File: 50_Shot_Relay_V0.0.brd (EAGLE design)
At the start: 110.7 x 130.5 mm, 183 parts, among them J1 J13, J2 J14, J3 J15, J4 J16, Q1 Qs5U34CT-ND, Q10 Qs5U34CT-ND, Q11 Qs5U34CT-ND, Q12 Qs5U34CT-ND, Q13 Qs5U34CT-ND, Q14 Qs5U34CT-ND, Q15 Qs5U34CT-ND, Q16 Qs5U34CT-ND, Q17 Qs5U34CT-ND, Q18 Qs5U34CT-ND, Q19 Qs5U34CT-ND, Q2 Qs5U34CT-ND, Q20 Qs5U34CT-ND, Q21 Qs5U34CT-ND, Q22 Qs5U34CT-ND, Q23 Qs5U34CT-ND, Q24 Qs5U34CT-ND, Q25 Qs5U34CT-ND, Q26 Qs5U34CT-ND, Q27 Qs5U34CT-ND, Q28 Qs5U34CT-ND, Q29 Qs5U34CT-ND, Q3 Qs5U34CT-ND, Q30 Qs5U34CT-ND, Q4 Qs5U34CT-ND, Q5 Qs5U34CT-ND, Q6 Qs5U34CT-ND, Q7 Qs5U34CT-ND, Q8 Qs5U34CT-ND, Q9 Qs5U34CT-ND, U1 MM74HC595, U2 MM74HC595, U3 7400, U4 MM74HC245, U5 MM74HC245, U6 ULN2803ADW, U7 ULN2803ADW, X1 22-23-2111, X2 22-23-2111, X3 22-23-2091, X4 22-23-2031, X5 22-23-2101, X6 22-23-2101

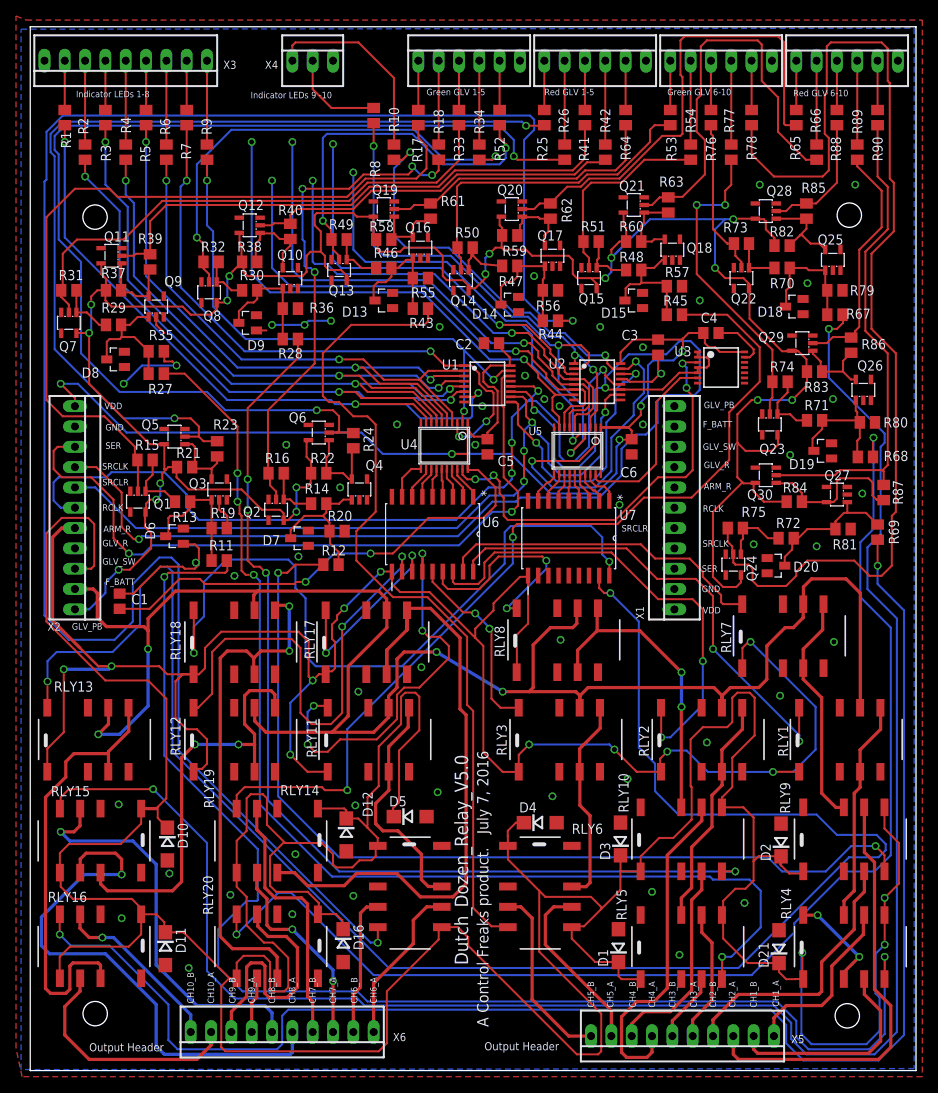
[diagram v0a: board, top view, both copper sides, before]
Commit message: add proper relay board
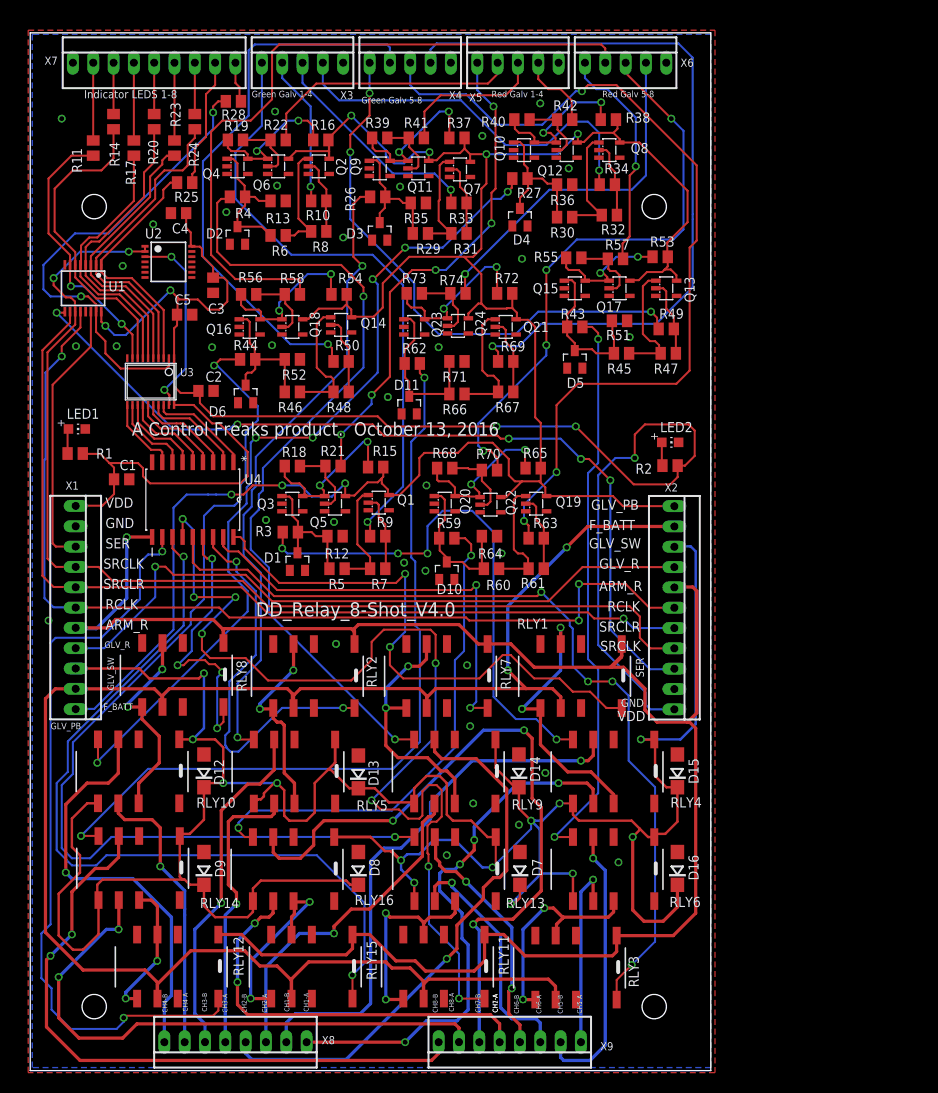
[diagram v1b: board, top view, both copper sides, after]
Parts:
- removed C6: 0.01uF, rcl:C0805
- removed D18, D19, D20: 5.0V, Mine:SOT23
- removed D21: SA2M-E3/5ATGICT-ND, Mine:DO214AC
- removed J1: J13, Mine:22-23-2061
- removed J2: J14, Mine:22-23-2061
- removed J3: J15, Mine:22-23-2061
- removed J4: J16, Mine:22-23-2061
- removed Q25, Q26, Q27, Q28, Q29, Q30: Qs5U34CT-ND, Mine:SOT23-5L
- removed R75: 1M, rcl:M0805
- removed R76, R77, R78, R88, R89, R90: 1k, rcl:M0805
- removed R79, R80, R81, R85, R86, R87: 100k, rcl:M0805
- removed R82, R83, R84: 10k, rcl:M0805
- removed RLY17, RLY18, RLY19, RLY20: OMRON, Mine:OMRONG6S
- removed U5: MM74HC245, Mine:TSSOP20
- removed U6, U7: ULN2803ADW, Texas Instruments_By_element14_Batch_1:SOIC127P1030X265-18N
- added LED1, LED2: LEDCHIP-LED0805, Mine:CHIP-LED0805
- added X7: 22-23-2091, Mine:22-23-2091
- added X8, X9: 22-23-2081, Mine:22-23-2081
- C1: value .01uf -> 0.01uF
- D1, D10, D11, D2, D3, D4, D5: value SA2M-E3/5ATGICT-ND -> 5.0V; device Mine:DO214AC -> Mine:SOT23
- D13, D14, D15, D7, D8, D9: value 5.0V -> SA2M-E3/5ATGICT-ND; device Mine:SOT23 -> Mine:DO214AC
- R1, R2: value 330 -> 100
- R10: value 560 -> 1k
- R11, R28: value 10k -> 330
- R12, R45, R60, R68: value 10k -> 100k
- R14, R20, R23, R24: value 100k -> 330
- R15, R16: value 1M -> 10k
- R17, R25: value 1k -> 330
- R18, R52, R64, R66: value 1k -> 100k
- R21, R22, R58, R69: value 10k -> 1k
- R26, R53, R54, R65: value 1k -> 10k
- R3, R4: value 330 -> 10k
- R47, R48, R61: value 100k -> 1M
- R49, R50, R74: value 1M -> 1k
- R5, R6: value 330 -> 100k
- R51, R73: value 1M -> 100k
- R57, R63, R70: value 100k -> 1k
- R62, R72: value 100k -> 10k
- R67: value 10k -> 1M
- R7: value 330 -> 1M
- R8: value 560 -> 1M
- R9: value 330 -> 1k
- U2: value MM74HC595 -> 7400; device Mine:TSSOP16 -> 74xx-us:TSSOP14
- U3: value 7400 -> MM74HC245; device 74xx-us:TSSOP14 -> Mine:TSSOP20
- U4: value MM74HC245 -> ULN2803ADW; device Mine:TSSOP20 -> Texas Instruments_By_element14_Batch_1:SOIC127P1030X265-18N
- X3: value 22-23-2091 -> 22-23-2051; device Mine:22-23-2091 -> Mine:22-23-2051
- X4: value 22-23-2031 -> 22-23-2051; device Mine:22-23-2031 -> Mine:22-23-2051
- X5, X6: value 22-23-2101 -> 22-23-2051; device con-molex:22-23-2101 -> Mine:22-23-2051
- moved X6 128.5 mm to (74.4, 126.0), turned to 0 degrees
- moved X5 123.4 mm to (61.0, 126.0), turned to 0 degrees
- moved D2 101.6 mm to (25.9, 104.4), turned to 0 degrees
- moved R2 83.0 mm to (80.0, 75.6), turned to 0 degrees
- moved D3 81.7 mm to (43.7, 104.9), turned to 0 degrees
- moved X2 76.0 mm to (80.5, 57.9)
- moved X1 75.9 mm to (5.68, 57.9), turned to 270 degrees
- moved D4 75.7 mm to (61.2, 106.7)
- moved D11 74.5 mm to (47.4, 83.2), turned to 0 degrees
- moved U3 71.4 mm to (15.0, 86.1), turned to 180 degrees
- moved D8 70.5 mm to (41.0, 25.3)
- moved D9 68.4 mm to (21.7, 25.3)
- moved C4 68.2 mm to (18.5, 107.2), turned to 180 degrees
- moved RLY10 64.3 mm to (15.4, 35.6), turned to 180 degrees
- moved D1 62.6 mm to (33.4, 63.6), turned to 0 degrees
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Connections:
- removed net CH10_A: RLY16.6, X6.9
- removed net CH10_B: RLY16.3, X6.10
- removed net CH9_A: RLY20.6, X6.7
- removed net CH9_B: RLY20.3, X6.8
- removed net GLV10_GRN: J2.5, R78.1
- removed net GLV10_RED: J4.5, R90.1
- removed net GLV9_GRN: J2.4, R77.1
- removed net GLV9_RED: J4.4, R89.1
- removed net GLV_10: R69.2, RLY16.4
- removed net GLV_9: R68.2, RLY20.4
- removed net N$101: RLY18.3, RLY18.5, RLY20.7
- removed net N$162: D19.3, Q26.1, R68.1, R71.2, R80.2
- removed net N$163: Q23.1, R71.1, R74.2
- removed net N$164: Q23.2, R74.1, R77.2
- removed net N$165: Q26.5, Q29.1, R83.1, R86.2
- removed net N$166: Q29.2, R86.1, R89.2
- removed net N$169: D20.3, Q27.1, R69.1, R72.2, R81.2
- removed net N$170: Q24.1, R72.1, R75.2
- removed net N$171: Q24.2, R75.1, R78.2
- removed net N$172: Q27.5, Q30.1, R84.1, R87.2
- removed net N$173: Q30.2, R87.1, R90.2
- removed net N$179: R3.1, X3.6
- removed net N$180: R2.1, X3.7
- removed net N$181: R1.1, X3.8
- removed net N$182: R10.1, X4.1
- removed net N$183: R8.1, X4.2
- removed net N$19: R10.2, U2.15, U5.2
- removed net N$20: R8.2, U2.1, U5.3
- removed net N$21: U1.9, U2.14
- removed net N$22: U2.2, U5.4
- removed net N$23: U2.3, U5.5
- removed net N$24: U2.4, U5.6
- removed net N$25: U2.5, U5.7
- removed net N$26: U2.6, U5.8
- removed net N$27: U2.7, U5.9
- removed net N$35: U5.18, U7.1
- removed net N$36: U5.17, U7.2
- removed net N$37: U5.16, U7.3
- removed net N$38: U5.15, U7.4
- removed net N$39: U5.14, U7.5
- removed net N$40: U5.13, U7.6
- removed net N$41: U5.12, U7.7
- removed net N$42: U5.11, U7.8
- removed net N$44: U3.6, U5.19
- removed net N$52: RLY18.8, U7.18
- removed net N$53: RLY13.8, U7.17
- removed net N$54: X1.8
- removed net N$55: X1.9
- removed net N$56: X1.10
- removed net N$57: X1.11
- removed net N$7: X1.6
- removed net N$8: X1.7
- removed net N$91: RLY13.3, RLY13.5, RLY16.7
- new net QN_ALT: U1.9, X2.9
- net ARM_RELAY: now also RLY15.1, U4.10, X1.7, X2.5; no longer RLY13.1, RLY17.1, RLY18.1, U6.10, U7.10, X2.7
- net CH1_A: now also X8.1; no longer X5.1
- net CH1_B: now also X8.2; no longer X5.2
- net CH2_A: now also X8.3; no longer X5.3
- net CH2_B: now also X8.4; no longer X5.4
- net CH3_A: now also X8.5; no longer X5.5
- net CH3_B: now also X8.6; no longer X5.6
- net CH4_A: now also X8.7; no longer X5.7
- net CH4_B: now also X8.8; no longer X5.8
- net CH5_A: now also X9.1; no longer X5.9
- net CH5_B: now also X9.2; no longer X5.10
- net CH6_A: now also RLY13.6, X9.3; no longer RLY14.6, X6.1
- net CH6_B: now also RLY13.3, X9.4; no longer RLY14.3, X6.2
- net CH7_A: now also RLY16.6, X9.5; no longer RLY19.6, X6.3
- net CH7_B: now also RLY16.3, X9.6; no longer RLY19.3, X6.4
- net CH8_A: now also RLY14.6, X9.7; no longer RLY15.6, X6.5
- net CH8_B: now also RLY14.3, X9.8; no longer RLY15.3, X6.6
- net F_BATT: now also RLY15.6, X1.10, X2.2; no longer RLY13.6, RLY17.6, RLY18.6, X2.10
- net GLV1_GRN: now also R9.1, X3.1; no longer J1.1, R17.1
- net GLV1_RED: now also R21.1, X5.1; no longer J3.1, R25.1
- net GLV2_GRN: now also R10.1, X3.2; no longer J1.2, R18.1
- net GLV2_RED: now also R22.1, X5.2; no longer J3.2, R26.1
- net GLV3_GRN: now also X3.3; no longer J1.3
- net GLV3_RED: now also X5.3; no longer J3.3
- net GLV4_GRN: now also X3.4; no longer J1.4
- net GLV4_RED: now also X5.4; no longer J3.4
- net GLV5_GRN: now also R49.1, X4.1; no longer J1.5, R52.1
- net GLV5_RED: now also R57.1, X6.1; no longer J3.5, R64.1
- net GLV6_GRN: now also R50.1, X4.2; no longer J2.1, R53.1
- net GLV6_RED: now also R58.1, X6.2; no longer J4.1, R65.1
- net GLV7_GRN: now also R63.1, X4.3; no longer J2.2, R54.1
- net GLV7_RED: now also R70.1, X6.3; no longer J4.2, R66.1
- net GLV8_GRN: now also R69.1, X4.4; no longer J2.3, R76.1
- net GLV8_RED: now also R74.1, X6.4; no longer J4.3, R88.1
- net GLV_1: now also R3.2; no longer R11.2
- net GLV_2: now also R4.2; no longer R12.2
- net GLV_3: now also R26.2; no longer R27.2
- net GLV_4: now also R27.2; no longer R28.2
- net GLV_6: now also RLY13.4; no longer RLY14.4
- net GLV_7: now also R59.2, RLY16.4; no longer R45.2, RLY19.4
- net GLV_8: now also R62.2, RLY14.4; no longer R67.2, RLY15.4
- net GLV_PB: now also Q17.5, Q18.5, R15.2, R16.2, R53.2, R54.2, R65.2, R72.2, X1.11, X2.1; no longer Q15.5, Q20.5, Q23.5, Q28.5, Q29.5, Q30.5, R21.2, R22.2, R58.2, R59.2, R60.2, R82.2, R83.2, R84.2, X2.11
- net GLV_RELAY: now also X1.8, X2.4; no longer X2.8
- net GLV_SW: now also D13.C, D14.C, D15.C, D7.C, D8.C, D9.C, RLY13.1, RLY13.5, X1.9, X2.3; no longer D1.C, D10.C, D11.C, D2.C, D21.C, D3.C, D4.C, D5.C, RLY15.1, RLY15.5, RLY19.1, RLY19.5, RLY20.1, RLY20.5, X2.9
- net GND: now also D1.1, D10.1, D11.1, D13.A, D14.A, D15.A, D2.1, D3.1, D4.1, D5.1, D7.A, D8.A, D9.A, LED1.C, LED2.C, Q15.2, Q20.2, Q23.2, R12.1, R13.1, R51.1, R52.1, R64.1, R71.1, RLY13.8, U2.10, U2.12, U2.4, U2.5, U2.7, U2.9, U4.9, X1.2, X2.10, X3.5, X4.5, X5.5, X6.5, X7.1; no longer C6.2, D1.A, D10.A, D11.A, D13.1, D14.1, D15.1, D18.1, D19.1, D2.A, D20.1, D21.A, D3.A, D4.A, D5.A, D7.1, D8.1, D9.1, J1.6, J2.6, J3.6, J4.6, Q17.2, Q18.2, Q25.2, Q26.2, Q27.2, R19.1, R20.1, R55.1, R56.1, R57.1, R79.1, R80.1, R81.1, RLY15.8, RLY17.2, RLY18.2, RLY19.2, RLY19.8, RLY20.2, RLY20.8, U2.8, U3.12, U3.13, U3.7, U3.9, U4.10, U5.10, U6.9, U7.9, X2.2, X3.9, X4.3
- net N$1: now also LED2.A, R2.1; no longer X1.1
- net N$10: now also R25.2, U3.3; no longer R7.2, U4.3
- net N$106: now also D1.3, R12.2, R3.1, R5.2; no longer D6.3, R11.1, R13.2, R19.2
- net N$107: now also R5.1, R7.2; no longer R13.1, R15.2
- net N$108: now also R18.1, R21.2; no longer R23.1, R25.2
- net N$109: now also R7.1, R9.2; no longer R15.1, R17.2
- net N$11: now also R24.2, U3.4; no longer R6.2, U4.4
- net N$110: now also R15.1, R18.2; no longer R21.1, R23.2
- net N$114: now also D2.3, R13.2, R4.1, R6.2; no longer D7.3, R12.1, R14.2, R20.2
- net N$115: now also R6.1, R8.2; no longer R14.1, R16.2
- net N$116: now also R10.2, R8.1; no longer R16.1, R18.2
- net N$117: now also R16.1, R19.2; no longer R22.1, R24.2
- net N$118: now also R19.1, R22.2; no longer R24.1, R26.2
- net N$12: now also R23.2, U3.5; no longer R5.2, U4.5
- net N$120: now also D3.3, R26.1; no longer D8.3, R27.1
- net N$127: now also D4.3, R27.1; no longer D9.3, R28.1
- net N$13: now also R20.2, U3.6; no longer R4.2, U4.6
- net N$134: now also D10.3, Q20.1, R59.1, R60.2, R64.2; no longer D15.3, Q18.1, R45.1, R48.2, R57.2
- net N$135: now also Q19.1, R60.1, R61.2; no longer Q15.1, R48.1, R51.2
- net N$136: now also Q19.2, R61.1, R63.2; no longer Q15.2, R51.1, R54.2
- net N$137: now also Q20.5, Q22.1, R65.1, R68.2; no longer Q18.5, Q21.1, R60.1, R63.2
- net N$138: now also Q22.2, R68.1, R70.2; no longer Q21.2, R63.1, R66.2
- net N$14: now also R17.2, U3.7; no longer R3.2, U4.7
- net N$141: now also D6.3, Q16.1, R46.2, R52.2; no longer D14.3, Q17.1, R47.2, R56.2
- net N$142: now also R46.1, R48.2; no longer R47.1, R50.2
- net N$143: now also R48.1, R50.2; no longer R50.1, R53.2
- net N$144: now also Q16.5, Q18.1, R54.1, R56.2; no longer Q17.5, Q20.1, R59.1, R62.2
- net N$145: now also Q18.2, R56.1, R58.2; no longer Q20.2, R62.1, R65.2
- net N$148: now also D5.3, Q15.1, R45.2, R51.2; no longer D13.3, Q16.1, R46.2, R55.2
- net N$149: now also R45.1, R47.2; no longer R46.1, R49.2
- net N$15: now also R14.2, U3.8; no longer R2.2, U4.8
- net N$150: now also R47.1, R49.2; no longer R49.1, R52.2
- net N$151: now also Q15.5, Q17.1, R53.1, R55.2; no longer Q16.5, Q19.1, R58.1, R61.2
- net N$152: now also Q17.2, R55.1, R57.2; no longer Q19.2, R61.1, R64.2
- net N$155: now also D11.3, Q23.1, R62.1, R66.2, R71.2; no longer D18.3, Q25.1, R67.1, R70.2, R79.2
- net N$156: now also Q21.1, R66.1, R67.2; no longer Q22.1, R70.1, R73.2
- net N$157: now also Q21.2, R67.1, R69.2; no longer Q22.2, R73.1, R76.2
- net N$158: now also Q23.5, Q24.1, R72.1, R73.2; no longer Q25.5, Q28.1, R82.1, R85.2
- net N$159: now also Q24.2, R73.1, R74.2; no longer Q28.2, R85.1, R88.2
- net N$16: now also R11.2, U3.9; no longer R1.2, U4.9
- net N$17: now also U3.18, U4.1; no longer U4.18, U6.1
- net N$174: now also R28.1, X7.9; no longer R9.1, X3.1
- net N$175: now also R25.1, X7.8; no longer R7.1, X3.2
- net N$176: now also R24.1, X7.7; no longer R6.1, X3.3
- net N$177: now also R23.1, X7.6; no longer R5.1, X3.4
- net N$178: now also R20.1, X7.5; no longer R4.1, X3.5
- net N$18: now also U2.3, U3.19; no longer U3.3, U4.19
- net N$2: now also R17.1, X7.4; no longer X1.2
- net N$28: now also U3.17, U4.2; no longer U4.17, U6.2
- net N$29: now also U3.16, U4.3; no longer U4.16, U6.3
- net N$3: now also R14.1, X7.3; no longer X1.3
- net N$30: now also U3.15, U4.4; no longer U4.15, U6.4
- net N$31: now also U3.14, U4.5; no longer U4.14, U6.5
- net N$32: now also U3.13, U4.6; no longer U4.13, U6.6
- net N$33: now also U3.12, U4.7; no longer U4.12, U6.7
- net N$34: now also U3.11, U4.8; no longer U4.11, U6.8
- net N$4: now also LED1.A, R1.2; no longer X1.4
- net N$43: now also U4.18; no longer U6.18
- net N$45: now also U4.17; no longer U6.17
- net N$46: now also U4.16; no longer U6.16
- net N$47: now also U4.15; no longer U6.15
- net N$48: now also U4.14; no longer U6.14
- net N$49: now also U4.13; no longer U6.13
- net N$5: now also R11.1, X7.2; no longer X1.5
- net N$50: now also RLY15.8, U4.12; no longer RLY17.8, U6.12
- net N$51: now also U4.11; no longer U6.11
- net N$80: now also RLY13.7; no longer RLY14.7
- net N$87: now also RLY14.7; no longer RLY15.7
- net N$9: now also R28.2, U3.2; no longer R9.2, U4.2
- net N$94: now also RLY15.3, RLY15.5, RLY16.7; no longer RLY17.3, RLY17.5, RLY19.7
- net RCLK: now also X1.6; no longer U2.12
- net SER: now also X1.3; no longer X2.3
- net SRCLK: now also U2.1, U2.2, X1.4, X2.8; no longer U2.11, U3.1, U3.2, U3.4, U3.5, X2.4
- net SRCLR: now also X1.5, X2.7; no longer U2.10, X2.5
- net VDD: now also R1.1, R2.2, U2.14, U3.1, U3.20, X1.1, X2.11; no longer C6.1, U2.16, U3.14, U4.1, U4.20, U5.1, U5.20, X2.1
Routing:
- net N$53: track 221.0 -> 0.00 mm, vias 2 -> 0
- net GLV_SW: track 552.6 -> 362.0 mm, vias 3 -> 13
- net GLV_10: track 189.3 -> 0.00 mm, vias 2 -> 0
- net GLV_9: track 154.5 -> 0.00 mm, vias 2 -> 0
- net N$171: track 135.8 -> 0.00 mm
- net GLV_8: track 228.2 -> 98.1 mm
- net N$118: track 136.5 -> 8.28 mm, vias 2 -> 0
- net GLV_6: track 240.0 -> 123.7 mm
- net QN_ALT: track 0.00 -> 108.3 mm, vias 0 -> 5
- net N$108: track 117.3 -> 9.38 mm, vias 2 -> 0
- net GLV_1: track 168.0 -> 66.8 mm, vias 2 -> 4
- net GLV7_GRN: track 10.5 -> 109.9 mm, vias 0 -> 3
- net N$52: track 92.4 -> 0.00 mm, vias 2 -> 0
- net N$19: track 90.9 -> 0.00 mm, vias 4 -> 0
- net N$109: track 98.7 -> 9.80 mm
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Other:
- board size 110.7 x 130.5 mm -> 85.1 x 129.7 mm
- board text added: "A Control Freaks product. October 13, 2016"
- board text added: "CH1-A"
- board text added: "CH1-B"
- board text added: "CH2-A"
- board text added: "CH2-B"
- board text added: "CH3-A"
- board text added: "CH3-B"
- board text added: "CH4-A"
- board text added: "CH4-B"
- board text added: "CH5-A"
- board text added: "CH5-B"
- board text added: "CH6-A"
- board text added: "CH6-B"
- board text added: "CH7-A"
- board text added: "CH7-B"
- board text added: "CH8-A"
- board text added: "CH8-B"
- board text added: "DD_Relay_8-Shot_V4.0"
- board text added: "Green Galv 1-4"
- board text added: "Green Galv 5-8"
- board text added: "Indicator LEDS 1-8"
- board text added: "Red Galv 1-4"
- board text added: "Red Galv 5-8"
- board text removed: "A Control Freaks product. July 7, 2016"
- board text removed: "CH10_A"
- board text removed: "CH10_B"
- board text removed: "CH1_A"
- board text removed: "CH1_B"
- board text removed: "CH2_A"
- board text removed: "CH2_B"
- board text removed: "CH3_A"
- board text removed: "CH3_B"
- board text removed: "CH4_A"
- board text removed: "CH4_B"
- board text removed: "CH5_A"
- board text removed: "CH5_B"
- board text removed: "CH6_A"
- board text removed: "CH6_B"
- board text removed: "CH7_A"
- board text removed: "CH7_B"
- board text removed: "CH8_A"
- board text removed: "CH8_B"
- board text removed: "CH9_A"
- board text removed: "CH9_B"
- board text removed: "Dutch_Dozen_Relay_V5.0"
- board text removed: "Green GLV 1-5"
- board text removed: "Green GLV 6-10"
- board text removed: "Indicator LEDs 1-8"
- board text removed: "Indicator LEDs 9 -10"
- board text removed: "Output Header"
- board text removed: "Red GLV 1-5"
- board text removed: "Red GLV 6-10"
